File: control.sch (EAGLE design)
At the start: 65 parts, among them IC3 ATTINY85-20S

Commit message: FAIL compact layout
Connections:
- removed net B0: IC3.(MOSI/DI/SDA/AIN0/OC0A/OC1A/AREF/PCINT0)PB0, SL1.5
- removed net B1: IC3.(MISO/DO/AIN1/OC0B/OC1A/PCINT1)PB1, SL1.6
- removed net B2: IC3.(SCK/USCK/SCL/ADC1/T0/INT0/PCINT2)PB2
- removed net N$39: SL1.3
- new net ENC1: IC3.(MISO/DO/AIN1/OC0B/OC1A/PCINT1)PB1, SL1.5
- new net ENC2: IC3.(SCK/USCK/SCL/ADC1/T0/INT0/PCINT2)PB2, SL1.6
- new net ENCOUT: IC3.(MOSI/DI/SDA/AIN0/OC0A/OC1A/AREF/PCINT0)PB0, U$1.USB1_N
- net 3V3: now also SL1.3
- net LEDSTR_1: now also U$44.P$9; no longer U$44.P$1
- net LEDSTR_11: now also U$44.P$1; no longer U$44.P$9
- net LEDSTR_2: now also U$44.P$8; no longer U$44.P$2
- net LEDSTR_3: now also U$44.P$7; no longer U$44.P$3
- net LEDSTR_4: now also U$44.P$6; no longer U$44.P$4
- net LEDSTR_5: now also U$44.P$3; no longer U$44.P$7
- net LEDSTR_6: now also U$44.P$4; no longer U$44.P$6
- net LEDSTR_8: now also U$44.P$2; no longer U$44.P$8
- net ZN0: now also U$37.LED7; no longer U$37.LED0
- net ZN1: now also U$37.LED6; no longer U$37.LED1
- net ZN2: now also U$37.LED5; no longer U$37.LED2
- net ZN3: now also U$37.LED4; no longer U$37.LED3
- net ZN4: now also U$37.LED3; no longer U$37.LED4
- net ZN5: now also U$37.LED2; no longer U$37.LED5
- net ZN6: now also U$37.LED1; no longer U$37.LED6
- net ZN7: now also U$37.LED0; no longer U$37.LED7

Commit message: completes first ideration
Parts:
- removed U$43: 2N7002P, LED Driver:2N7002P
- added SL2: (no value), con-amp-quick:M07
- added U$38: 2N7002P, Smile_Shade:2N7002P
- U$10, U$12, U$14, U$16, U$18, U$20, U$22, U$24, U$26, U$28, U$30, U$32, U$34, U$4, U$41, U$6, U$8: device LED Driver:2N7002P -> Smile_Shade:2N7002P
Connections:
- removed net 24V: U$2.VCC2
- new net +3V3: IC3.VCC
- new net ENDSTOP0: SL2.3, U$1.CSID0
- new net ENDSTOP1: SL2.4, U$1.CSID1
- new net ENDSTOP2: SL2.5, U$1.CSID2
- new net ENDSTOP3: SL2.6, U$1.CSID3
- net 3V3: now also SL2.7, U$2.VCC1; no longer IC3.VCC
- net 48V: now also SL2.1
- net 5V: now also U$2.VCC2; no longer U$2.VCC1
- net ENCOUT: now also U$1.UART2-TX; no longer U$1.USB1_N
- net GND: now also SL2.2, U$38.DRAIN; no longer U$43.DRAIN
- net LEDSTR_1: now also U$44.P$1; no longer U$44.P$9
- net LEDSTR_11: now also U$44.P$11; no longer U$44.P$1
- net LEDSTR_2: now also U$44.P$2; no longer U$44.P$8
- net LEDSTR_3: now also U$44.P$3; no longer U$44.P$7
- net LEDSTR_4: now also U$44.P$4; no longer U$44.P$6
- net LEDSTR_5: now also U$44.P$7; no longer U$44.P$3
- net LEDSTR_6: now also U$44.P$6; no longer U$44.P$4
- net LEDSTR_8: now also U$44.P$8; no longer U$44.P$2
- net LEDSTR_9: now also U$44.P$9; no longer U$44.P$11
- net N$11: now also U$12.SOURCE; no longer U$14.SOURCE
- net N$13: now also U$10.SOURCE; no longer U$16.SOURCE
- net N$15: now also U$38.SOURCE; no longer U$18.SOURCE
- net N$17: now also U$18.SOURCE; no longer U$20.SOURCE
- net N$19: now also U$20.SOURCE; no longer U$22.SOURCE
- net N$21: now also U$22.SOURCE; no longer U$24.SOURCE
- net N$23: now also U$24.SOURCE; no longer U$26.SOURCE
- net N$25: now also U$32.SOURCE; no longer U$28.SOURCE
- net N$29: now also U$28.SOURCE; no longer U$32.SOURCE
- net N$31: now also U$26.SOURCE; no longer U$34.SOURCE
- net N$35: now also U$34.SOURCE; no longer U$41.SOURCE
- net N$37: now also U$41.SOURCE; no longer U$43.SOURCE
- net N$7: now also U$16.SOURCE; no longer U$10.SOURCE
- net N$9: now also U$14.SOURCE; no longer U$12.SOURCE
- net ZN0: now also U$38.GATE; no longer U$18.GATE
- net ZN11: now also U$32.GATE; no longer U$28.GATE
- net ZN12: now also U$24.GATE; no longer U$26.GATE
- net ZN13: now also U$18.GATE; no longer U$20.GATE
- net ZN14: now also U$20.GATE; no longer U$22.GATE
- net ZN15: now also U$22.GATE; no longer U$24.GATE
- net ZN16: now also U$41.GATE; no longer U$43.GATE
- net ZN4: now also U$12.GATE; no longer U$14.GATE
- net ZN5: now also U$14.GATE; no longer U$12.GATE
- net ZN6: now also U$16.GATE; no longer U$10.GATE
- net ZN7: now also U$10.GATE; no longer U$16.GATE
- net ZN8: now also U$26.GATE; no longer U$41.GATE
- net ZN9: now also U$28.GATE; no longer U$32.GATE
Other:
- note removed: "Adafruit Trinket 3.3V"
- note removed: "CC 2.5 BY-SA"
- note removed: "http://adafruit.com/products/1500"

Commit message: adds actual route
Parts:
- removed SL2: (no value), con-amp-quick:M07
- added SL3: (no value), con-amp-quick:M09
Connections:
- net 3V3: now also SL3.7; no longer SL2.7
- net 48V: now also SL3.1; no longer SL2.1
- net ENDSTOP0: now also SL3.3; no longer SL2.3
- net ENDSTOP1: now also SL3.4; no longer SL2.4
- net ENDSTOP2: now also SL3.5; no longer SL2.5
- net ENDSTOP3: now also SL3.6; no longer SL2.6
- net GND: now also SL3.2; no longer SL2.2
- net M1A: now also SL3.8
- net M1B: now also SL3.9
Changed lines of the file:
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@@
 <part name="U$34" library="Smile_Shade" deviceset="2N7002P" device=""/>
 <part name="U$41" library="Smile_Shade" deviceset="2N7002P" device=""/>
-<part name="SL2" library="con-amp-quick" deviceset="M07" device=""/>
+<part name="SL3" library="con-amp-quick" deviceset="M09" device=""/>
 </parts>
 <sheets>
@@
 <instance part="U$37" gate="G$1" x="213.36" y="43.18"/>
 <instance part="SL1" gate="G$1" x="226.06" y="22.86" rot="R180"/>
-<instance part="SL2" gate="G$1" x="259.08" y="30.48" rot="R180"/>
+<instance part="SL3" gate="G$1" x="259.08" y="25.4" rot="R180"/>
 </instances>
 <busses>
@@
 <wire x1="83.82" y1="30.48" x2="88.9" y2="30.48" width="0.1524" layer="91"/>
 </segment>
+<segment>
+<pinref part="SL3" gate="G$1" pin="8"/>
+<wire x1="254" y1="17.78" x2="251.46" y2="17.78" width="0.1524" layer="91"/>
+</segment>
 </net>
 <net name="M2B" class="0">
@@
 <segment>
 <wire x1="251.46" y1="33.02" x2="254" y2="33.02" width="0.1524" layer="91"/>
-<pinref part="SL2" gate="G$1" pin="2"/>
+<pinref part="SL3" gate="G$1" pin="2"/>
 </segment>
 </net>
@@
 <wire x1="88.9" y1="22.86" x2="83.82" y2="22.86" width="0.1524" layer="91"/>
 <wire x1="83.82" y1="22.86" x2="83.82" y2="25.4" width="0.1524" layer="91"/>
+</segment>
+<segment>
+<pinref part="SL3" gate="G$1" pin="9"/>
+<wire x1="254" y1="15.24" x2="251.46" y2="15.24" width="0.1524" layer="91"/>
 </segment>
 </net>
@@
 <segment>
 <wire x1="254" y1="35.56" x2="251.46" y2="35.56" width="0.1524" layer="91"/>
-<pinref part="SL2" gate="G$1" pin="1"/>
+<pinref part="SL3" gate="G$1" pin="1"/>
 </segment>
 </net>
@@
 </segment>
 <segment>
-<pinref part="SL2" gate="G$1" pin="7"/>
 <wire x1="254" y1="20.32" x2="251.46" y2="20.32" width="0.1524" layer="91"/>
+<pinref part="SL3" gate="G$1" pin="7"/>
 </segment>
 </net>
@@
 <segment>
 <wire x1="254" y1="27.94" x2="251.46" y2="27.94" width="0.1524" layer="91"/>
-<pinref part="SL2" gate="G$1" pin="4"/>
+<pinref part="SL3" gate="G$1" pin="4"/>
 </segment>
 </net>
@@
 <segment>
 <wire x1="254" y1="25.4" x2="251.46" y2="25.4" width="0.1524" layer="91"/>
-<pinref part="SL2" gate="G$1" pin="5"/>
+<pinref part="SL3" gate="G$1" pin="5"/>
 </segment>
 </net>
@@
 <segment>
 <wire x1="254" y1="30.48" x2="251.46" y2="30.48" width="0.1524" layer="91"/>
-<pinref part="SL2" gate="G$1" pin="3"/>
+<pinref part="SL3" gate="G$1" pin="3"/>
 </segment>
 </net>
 <net name="ENDSTOP3" class="0">
 <segment>
-<pinref part="SL2" gate="G$1" pin="6"/>
 <wire x1="254" y1="22.86" x2="251.46" y2="22.86" width="0.1524" layer="91"/>
-</segment>
-</net>
+<pinref part="SL3" gate="G$1" pin="6"/>
+</segment>
+</net>

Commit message: fixes DRC err
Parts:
- removed R18: RC0603FR-0710RL, LED Driver:RC0603FR-0710RL
- removed U$35: LM2576HVT-5.0/NOPB, LED Driver:LM2576HVT-5.0/NOPB
- added R19: RC0603FR-0710RL, Smile_Shade:RC0603FR-0710RL
- added SL2: (no value), con-amp-quick:M02
- added U$43: LM2576HVSX-5.0/NOPB, Smile_Shade:LM2576HVSX-5.0/NOPB
- R1, R10, R11, R12, R13, R14, R15, R16, R17, R2, R3, R4, R5, R6, R7, R8, R9: device LED Driver:RC0603FR-0710RL -> Smile_Shade:RC0603FR-0710RL
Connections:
- new net N$39: SL2.1, U$1.I2SSPDIF
- new net N$40: SL2.2, U$1.I2SDO
- net 48: now also R16.22; no longer R17.22
- net 48V: now also R17.22, R19.22; no longer R16.22, R18.22
- net 5V: now also U$43.FB; no longer U$35.FB
- net GND: now also U$43.GND, U$43.TAB, U$43.~ON~/OFF; no longer U$35.!ON/OFF, U$35.GND
- net N$10: now also R4.11; no longer R5.11
- net N$12: now also R5.11; no longer R6.11
- net N$14: now also R6.11; no longer R7.11
- net N$18: now also R7.11; no longer R9.11
- net N$2: now also R19.11; no longer R1.11
- net N$20: now also R9.11; no longer R10.11
- net N$22: now also R10.11; no longer R11.11
- net N$24: now also R11.11; no longer R12.11
- net N$26: now also R15.11; no longer R13.11
- net N$30: now also R13.11; no longer R15.11
- net N$32: now also R12.11; no longer R16.11
- net N$33: now also U$43.OUT; no longer U$35.OUT
- net N$34: now also U$43.VIN; no longer U$35.VIN
- net N$36: now also R16.11; no longer R17.11
- net N$38: now also R17.11; no longer R18.11
- net N$4: now also R1.11; no longer R2.11
- net N$6: now also R2.11; no longer R3.11
- net N$8: now also R3.11; no longer R4.11

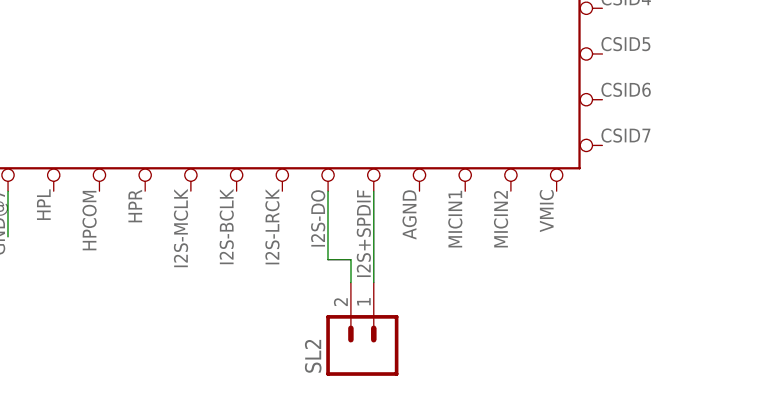
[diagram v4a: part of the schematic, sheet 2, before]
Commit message: adds ADC input with all RDC and  rounting
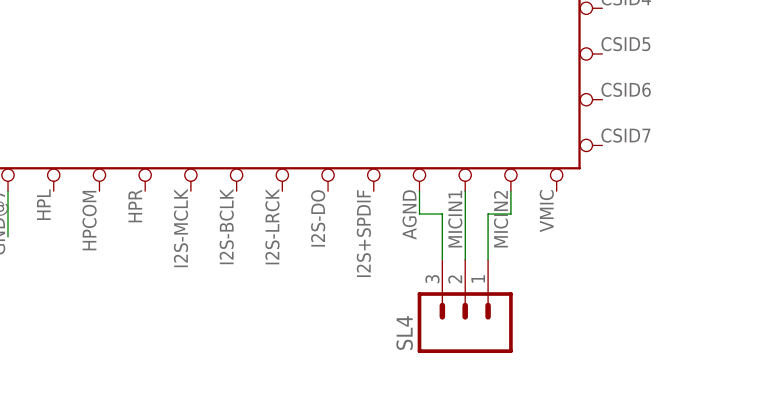
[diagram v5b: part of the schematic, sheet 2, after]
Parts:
- removed SL2: (no value), con-amp-quick:M02
- added SL4: (no value), con-amp-quick:M03
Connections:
- new net N$41: SL4.1, U$1.MICIN2
- net N$39: now also SL4.3, U$1.AGND; no longer SL2.1, U$1.I2SSPDIF
- net N$40: now also SL4.2, U$1.MICIN1; no longer SL2.2, U$1.I2SDO
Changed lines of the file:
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@@
 <part name="R16" library="Smile_Shade" deviceset="RC0603FR-0710RL" device=""/>
 <part name="R17" library="Smile_Shade" deviceset="RC0603FR-0710RL" device=""/>
-<part name="SL2" library="con-amp-quick" deviceset="M02" device=""/>
+<part name="SL4" library="con-amp-quick" deviceset="M03" device=""/>
 </parts>
 <sheets>
@@
 <instance part="IC3" gate="G$1" x="-60.96" y="60.96" rot="MR0"/>
 <instance part="GND22" gate="1" x="-27.94" y="50.8" rot="MR0"/>
-<instance part="SL2" gate="G$1" x="43.18" y="-20.32" rot="R90"/>
+<instance part="SL4" gate="G$1" x="53.34" y="-17.78" rot="R90"/>
 </instances>
 <busses>
@@
 <net name="N$39" class="0">
 <segment>
-<pinref part="U$1" gate="G$1" pin="I2SSPDIF"/>
-<pinref part="SL2" gate="G$1" pin="1"/>
-<wire x1="43.18" y1="-2.54" x2="43.18" y2="-12.7" width="0.1524" layer="91"/>
+<pinref part="U$1" gate="G$1" pin="AGND"/>
+<wire x1="48.26" y1="-2.54" x2="48.26" y2="-5.08" width="0.1524" layer="91"/>
+<pinref part="SL4" gate="G$1" pin="3"/>
+<wire x1="48.26" y1="-5.08" x2="50.8" y2="-5.08" width="0.1524" layer="91"/>
+<wire x1="50.8" y1="-5.08" x2="50.8" y2="-10.16" width="0.1524" layer="91"/>
 </segment>
 </net>
 <net name="N$40" class="0">
 <segment>
-<pinref part="U$1" gate="G$1" pin="I2SDO"/>
-<wire x1="38.1" y1="-2.54" x2="38.1" y2="-10.16" width="0.1524" layer="91"/>
-<wire x1="38.1" y1="-10.16" x2="40.64" y2="-10.16" width="0.1524" layer="91"/>
-<pinref part="SL2" gate="G$1" pin="2"/>
-<wire x1="40.64" y1="-10.16" x2="40.64" y2="-12.7" width="0.1524" layer="91"/>
-</segment>
-</net>
+<pinref part="U$1" gate="G$1" pin="MICIN1"/>
+<pinref part="SL4" gate="G$1" pin="2"/>
+<wire x1="53.34" y1="-2.54" x2="53.34" y2="-10.16" width="0.1524" layer="91"/>
+</segment>
+</net>
+<net name="N$41" class="0">
+<segment>
+<pinref part="U$1" gate="G$1" pin="MICIN2"/>
+<wire x1="58.42" y1="-2.54" x2="58.42" y2="-5.08" width="0.1524" layer="91"/>
+<pinref part="SL4" gate="G$1" pin="1"/>
+<wire x1="58.42" y1="-5.08" x2="55.88" y2="-5.08" width="0.1524" layer="91"/>
+<wire x1="55.88" y1="-5.08" x2="55.88" y2="-10.16" width="0.1524" layer="91"/>
+</segment>
+</net>
